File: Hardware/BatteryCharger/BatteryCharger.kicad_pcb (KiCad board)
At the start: 2 copper layers, 20 parts, among them J1 Wurth 691313510002, J2 Wurth 691313510002, Q1 TIP32C

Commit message: Progress - Laying out PCB
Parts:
- added H1: MountingHole_3.2mm_M3, MyParts:MountingHole_3.2mm_M3, F.Cu at (99.0, 90.0)
- added H2: MountingHole_3.2mm_M3, MyParts:MountingHole_3.2mm_M3, F.Cu at (158.0, 90.0)
- added H3: MountingHole_3.2mm_M3, MyParts:MountingHole_3.2mm_M3, F.Cu at (99.0, 119.0)
- added H4: MountingHole_3.2mm_M3, MyParts:MountingHole_3.2mm_M3, F.Cu at (158.0, 119.0)
- C3: value 01uF -> 0u1F
- moved R3 78.4 mm to (122.6, 116.8), turned to 0 degrees
- moved R11 68.3 mm to (137.2, 108.6)
- moved R10 62.0 mm to (147.3, 112.4), turned to 180 degrees
- moved R12 60.8 mm to (108.6, 109.2)
- moved C4 58.3 mm to (118.7, 104.8)
- moved R8 53.1 mm to (132.7, 113.0), turned to 180 degrees
- moved R4 53.0 mm to (147.3, 120.0)
- moved R9 52.7 mm to (137.2, 116.2)
- moved U1 39.9 mm to (128.3, 103.5)
- moved C3 38.2 mm to (137.2, 104.8)
- moved Q1 36.2 mm to (133.3, 88.6), turned to 0 degrees
- moved JP3 35.7 mm to (116.2, 95.9)
- moved JP2 35.4 mm to (141.0, 95.9)
- moved JP1 35.2 mm to (116.2, 100.3)
- moved R1 34.3 mm to (111.7, 90.2)
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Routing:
- net /Out: track 0.00 -> 64.6 mm
- net Net-(U1-VFB): track 0.00 -> 27.8 mm, vias 0 -> 1
- net Net-(JP1-B): track 0.00 -> 20.2 mm
- net Net-(U1-BSTOP): track 0.00 -> 17.6 mm
- net Net-(U1-/PGOOD): track 0.00 -> 16.8 mm, vias 0 -> 1
- net GND: track 0.00 -> 15.6 mm, vias 0 -> 1
- net Net-(JP2-C): track 0.00 -> 14.4 mm
- net Net-(Q1-B): track 0.00 -> 12.7 mm
- net Net-(JP1-A): track 0.00 -> 10.2 mm
- net Net-(D1-A): track 0.00 -> 7.77 mm
- net Net-(JP2-A): track 0.00 -> 7.22 mm
- net Net-(U1-COMP): track 0.00 -> 6.33 mm
- net Net-(U1-STAT1): track 0.00 -> 5.40 mm
- net Net-(U1-CE): track 0.00 -> 3.81 mm
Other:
- board outline added: 69 x 39 mm
- board text added: "BQ24450 Dev PCB SLA Charger"

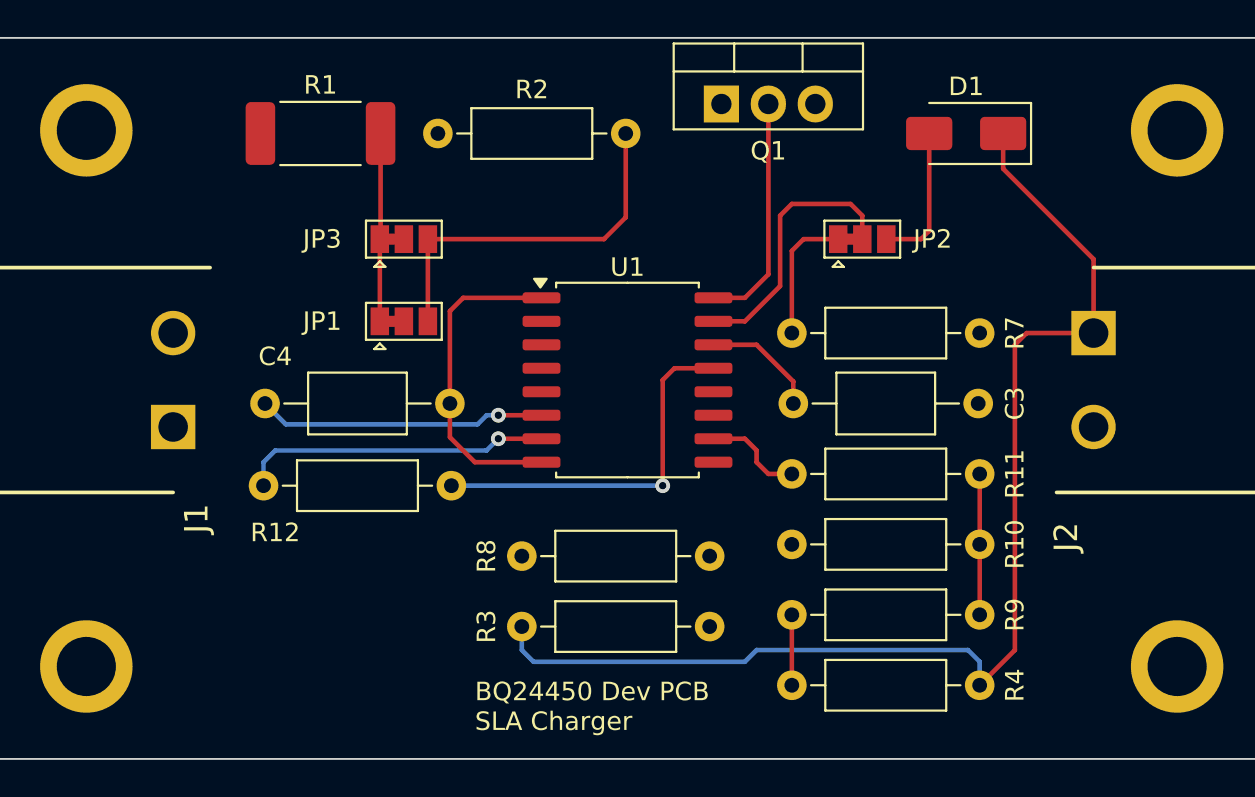
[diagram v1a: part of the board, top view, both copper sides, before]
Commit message: Initial PCB layout for charger
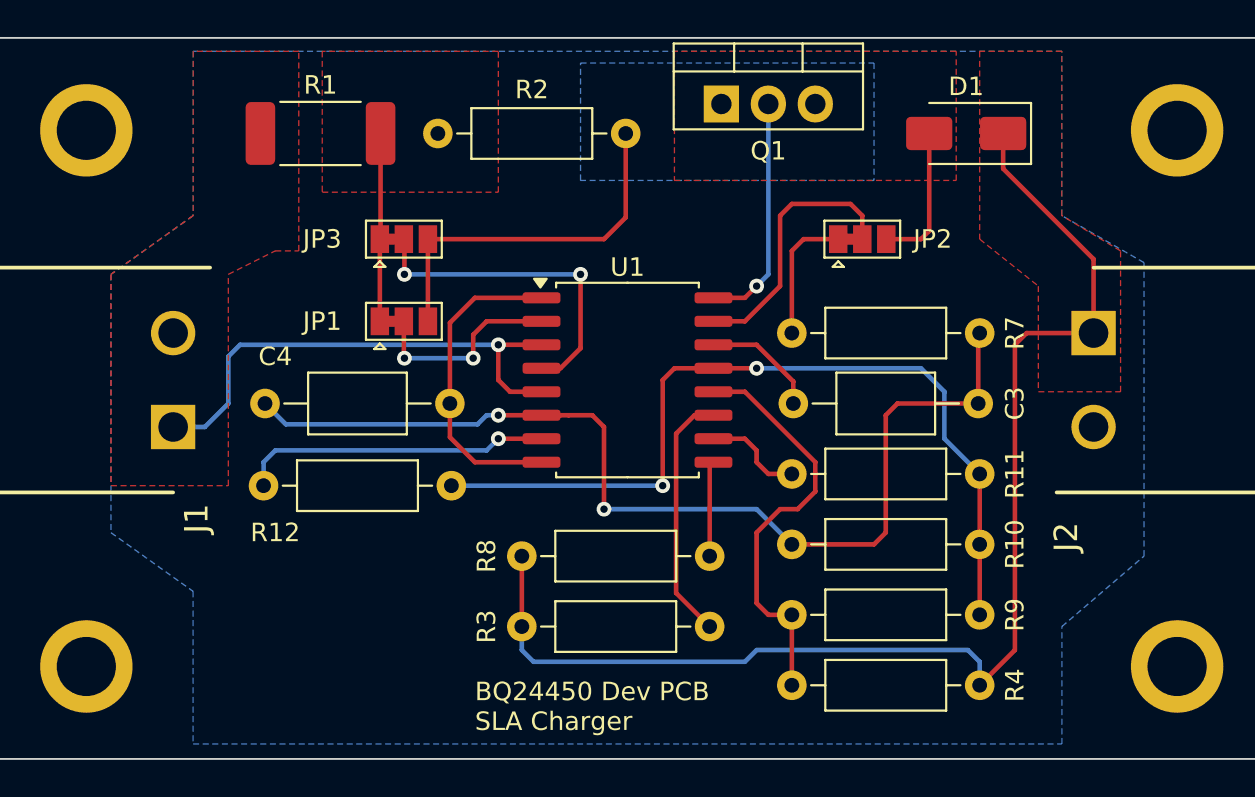
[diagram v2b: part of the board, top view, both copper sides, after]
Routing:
- net GND: track 15.6 -> 55.5 mm, vias 1 -> 2
- net /In: track 0.00 -> 27.8 mm, vias 0 -> 1
- net Net-(U1-CE): track 3.81 -> 22.6 mm
- net Net-(U1-VFB): track 27.8 -> 46.0 mm, vias 1 -> 2
- net Net-(JP3-C): track 0.00 -> 18.0 mm, vias 0 -> 2
- net Net-(U1-PRE-CHRG): track 0.00 -> 13.6 mm
- net Net-(JP1-C): track 0.00 -> 11.1 mm, vias 0 -> 2
- net Net-(U1-STAT2): track 0.00 -> 5.16 mm
- net /Out: track 64.6 -> 68.4 mm
- net Net-(Q1-B): vias 0 -> 1
- added copper zone on F.Cu, net /In
- added copper zone on F.Cu, net /Out
- added copper zone on B.Cu, net GND
- added copper zone on F.Cu, net Net-(D1-A)
- added copper zone on F.Cu, net Net-(JP1-A)
- added copper zone on B.Cu, net Net-(JP1-B)

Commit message: Board layout done, ready to check
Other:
- board text added: "+"
- board text added: "16-20V DC"
- board text added: "INPUT"
- board text added: "OUTPUT 12V SLA"
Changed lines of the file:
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@@
 		(tags "Connector")
 		(property "Reference" "J2"
-			(at 11.035 1.48 90)
+			(at -2.54 3.62 90)
 			(layer "F.SilkS")
 			(effects
@@
 		(tags "Connector")
 		(property "Reference" "J1"
-			(at -4.955 1.27 -90)
+			(at 7.62 3.62 -90)
 			(layer "F.SilkS")
 			(effects
@@
 		(layer "Edge.Cuts")
 	)
+	(gr_text "+"
+		(at 102.87 112.395 0)
+		(layer "F.SilkS")
+		(effects
+			(font
+				(size 1.5 1.5)
+				(thickness 0.3)
+				(bold yes)
+			)
+			(justify left bottom)
+		)
+	)
+	(gr_text "INPUT"
+		(at 94.615 112.395 0)
+		(layer "F.SilkS")
+		(effects
+			(font
+				(size 1.5 1.5)
+				(thickness 0.3)
+				(bold yes)
+			)
+			(justify left bottom)
+		)
+	)
+	(gr_text "+"
+		(at 152.4 96.52 0)
+		(layer "F.SilkS")
+		(effects
+			(font
+				(size 1.5 1.5)
+				(thickness 0.3)
+				(bold yes)
+			)
+			(justify left bottom)
+		)
+	)
 	(gr_text "BQ24450 Dev PCB\nSLA Charger"
 		(at 120.015 122.555 0)
@@
 			)
 			(justify left bottom)
+		)
+	)
+	(gr_text "16-20V DC"
+		(at 95.25 96.52 0)
+		(layer "F.SilkS")
+		(effects
+			(font
+				(size 1.5 1.5)
+				(thickness 0.3)
+				(bold yes)
+			)
+			(justify left bottom)
+		)
+	)
+	(gr_text "OUTPUT\n12V SLA"
+		(at 153.035 114.3 0)
+		(layer "F.SilkS")
+		(effects
+			(font
+				(size 1.5 1.5)
+				(thickness 0.3)
+				(bold yes)
+			)
+			(justify left bottom)

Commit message: Fix error on charger PCB and add mounting holes to schematic
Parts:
- H1, H2, H3, H4: value MountingHole_3.2mm_M3 -> MountingHole
- moved H2 65.7 mm to (99.0, 119.0)
- moved H3 65.7 mm to (158.0, 90.0)
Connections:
- Q1 pad 1: Net-(D1-A) -> Net-(Q1-B)
- Q1 pad 2: Net-(Q1-B) -> Net-(D1-A)
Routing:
- net Net-(Q1-B): track 12.7 -> 0.00 mm, vias 1 -> 0

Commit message: Charger: Minor PCB cleanup & generate manufacturing files
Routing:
- net GND: track 55.5 -> 3.52 mm, vias 2 -> 1
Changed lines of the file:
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@@
 		(allow_soldermask_bridges_in_footprints no)
 		(pcbplotparams
-			(layerselection 0x00010fc_ffffffff)
+			(layerselection 0x00010e0_ffffffff)
 			(plot_on_all_layers_selection 0x0000000_00000000)
 			(disableapertmacros no)
-			(usegerberextensions no)
-			(usegerberattributes yes)
-			(usegerberadvancedattributes yes)
-			(creategerberjobfile yes)
+			(usegerberextensions yes)
+			(usegerberattributes no)
+			(usegerberadvancedattributes no)
+			(creategerberjobfile no)
 			(dashed_line_dash_ratio 12.000000)
 			(dashed_line_gap_ratio 3.000000)
@@
 			(psa4output no)
 			(plotreference yes)
-			(plotvalue yes)
+			(plotvalue no)
 			(plotfptext yes)
 			(plotinvisibletext no)
 			(sketchpadsonfab no)
-			(subtractmaskfromsilk no)
+			(subtractmaskfromsilk yes)
 			(outputformat 1)
 			(mirror no)
-			(drillshape 1)
+			(drillshape 0)
 			(scaleselection 1)
-			(outputdirectory "")
+			(outputdirectory "Manufacturing/")
 		)
 	)
@@
 			(size 1.6 3.4)
 			(layers "F.Cu" "F.Paste" "F.Mask")
-			(roundrect_rratio 0.178571)
+			(roundrect_rratio 0.17857125)
 			(net 6 "/In")
 			(pintype "passive")
@@
 			(size 1.6 3.4)
 			(layers "F.Cu" "F.Paste" "F.Mask")
-			(roundrect_rratio 0.178571)
+			(roundrect_rratio 0.17857125)
 			(net 9 "Net-(JP1-A)")
 			(pintype "passive")
@@
 	)
 	(segment
-		(start 142.875 104.775)
-		(end 142.24 105.41)
-		(width 0.25)
-		(layer "F.Cu")
-		(net 2)
-	)
-	(segment
-		(start 124.644999 105.41)
-		(end 125.095 105.41)
-		(width 0.25)
-		(layer "F.Cu")
-		(net 2)
-	)
-	(segment
-		(start 125.095 105.41)
-		(end 126.365 105.41)
-		(width 0.25)
-		(layer "F.Cu")
-		(net 2)
-	)
-	(segment
-		(start 142.24 111.76)
-		(end 141.605 112.395)
-		(width 0.25)
-		(layer "F.Cu")
-		(net 2)
-	)
-	(segment
 		(start 147.24 101.045)
 		(end 147.32 100.965)
@@
 	)
 	(segment
-		(start 147.24 104.775)
-		(end 142.875 104.775)
-		(width 0.25)
-		(layer "F.Cu")
-		(net 2)
-	)
-	(segment
-		(start 127 106.045)
-		(end 127 110.49)
-		(width 0.25)
-		(layer "F.Cu")
-		(net 2)
-	)
-	(segment
 		(start 123.62 105.41)
-		(end 124.644999 105.41)
-		(width 0.25)
-		(layer "F.Cu")
-		(net 2)
-	)
-	(segment
-		(start 126.365 105.41)
-		(end 127 106.045)
-		(width 0.25)
-		(layer "F.Cu")
-		(net 2)
-	)
-	(segment
-		(start 147.24 104.775)
-		(end 147.24 101.045)
+		(end 126 105.41)
 		(width 0.25)
 		(layer "F.Cu")
@@
 	(segment
 		(start 123.62 105.41)
-		(end 121.285 105.41)
-		(width 0.25)
-		(layer "F.Cu")
-		(net 2)
-	)
-	(segment
-		(start 142.24 105.41)
-		(end 142.24 111.76)
-		(width 0.25)
-		(layer "F.Cu")
-		(net 2)
-	)
-	(segment
-		(start 141.605 112.395)
-		(end 137.16 112.395)
+		(end 124.644999 105.41)
 		(width 0.25)
 		(layer "F.Cu")
@@
 	)
 	(via
-		(at 121.285 105.41)
+		(at 126 105.41)
 		(size 0.8)
 		(drill 0.4)
@@
 		(net 2)
 	)
-	(via
-		(at 127 110.49)
-		(size 0.8)
-		(drill 0.4)
-		(layers "F.Cu" "B.Cu")
-		(net 2)
-	)
-	(segment
-		(start 109.79 105.9)
-		(end 108.665 104.775)
-		(width 0.25)
-		(layer "B.Cu")
-		(net 2)
-	)
-	(segment
-		(start 120.16 105.9)
-		(end 109.79 105.9)
-		(width 0.25)
-		(layer "B.Cu")
-		(net 2)
-	)
-	(segment
-		(start 135.255 110.49)
-		(end 137.16 112.395)
-		(width 0.25)
-		(layer "B.Cu")
-		(net 2)
-	)
-	(segment
-		(start 120.65 105.41)
-		(end 120.16 105.9)
-		(width 0.25)
-		(layer "B.Cu")
-		(net 2)
-	)
-	(segment
-		(start 127 110.49)
-		(end 135.255 110.49)
-		(width 0.25)
-		(layer "B.Cu")
-		(net 2)
-	)
-	(segment
-		(start 121.285 105.41)
-		(end 120.65 105.41)
-		(width 0.25)
-		(layer "B.Cu")
-		(net 2)
-	)
